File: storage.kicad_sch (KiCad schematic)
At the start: 18 parts, among them J6 Micro_SD_Card_Det1, U1 MIMX8MM6DVTLZAA, U25 TPD4EUSB30, U26 D5V0H1B2LP, U27 W25Q32JWZP, U28 SiP32431DR3, U29 TPD4EUSB30

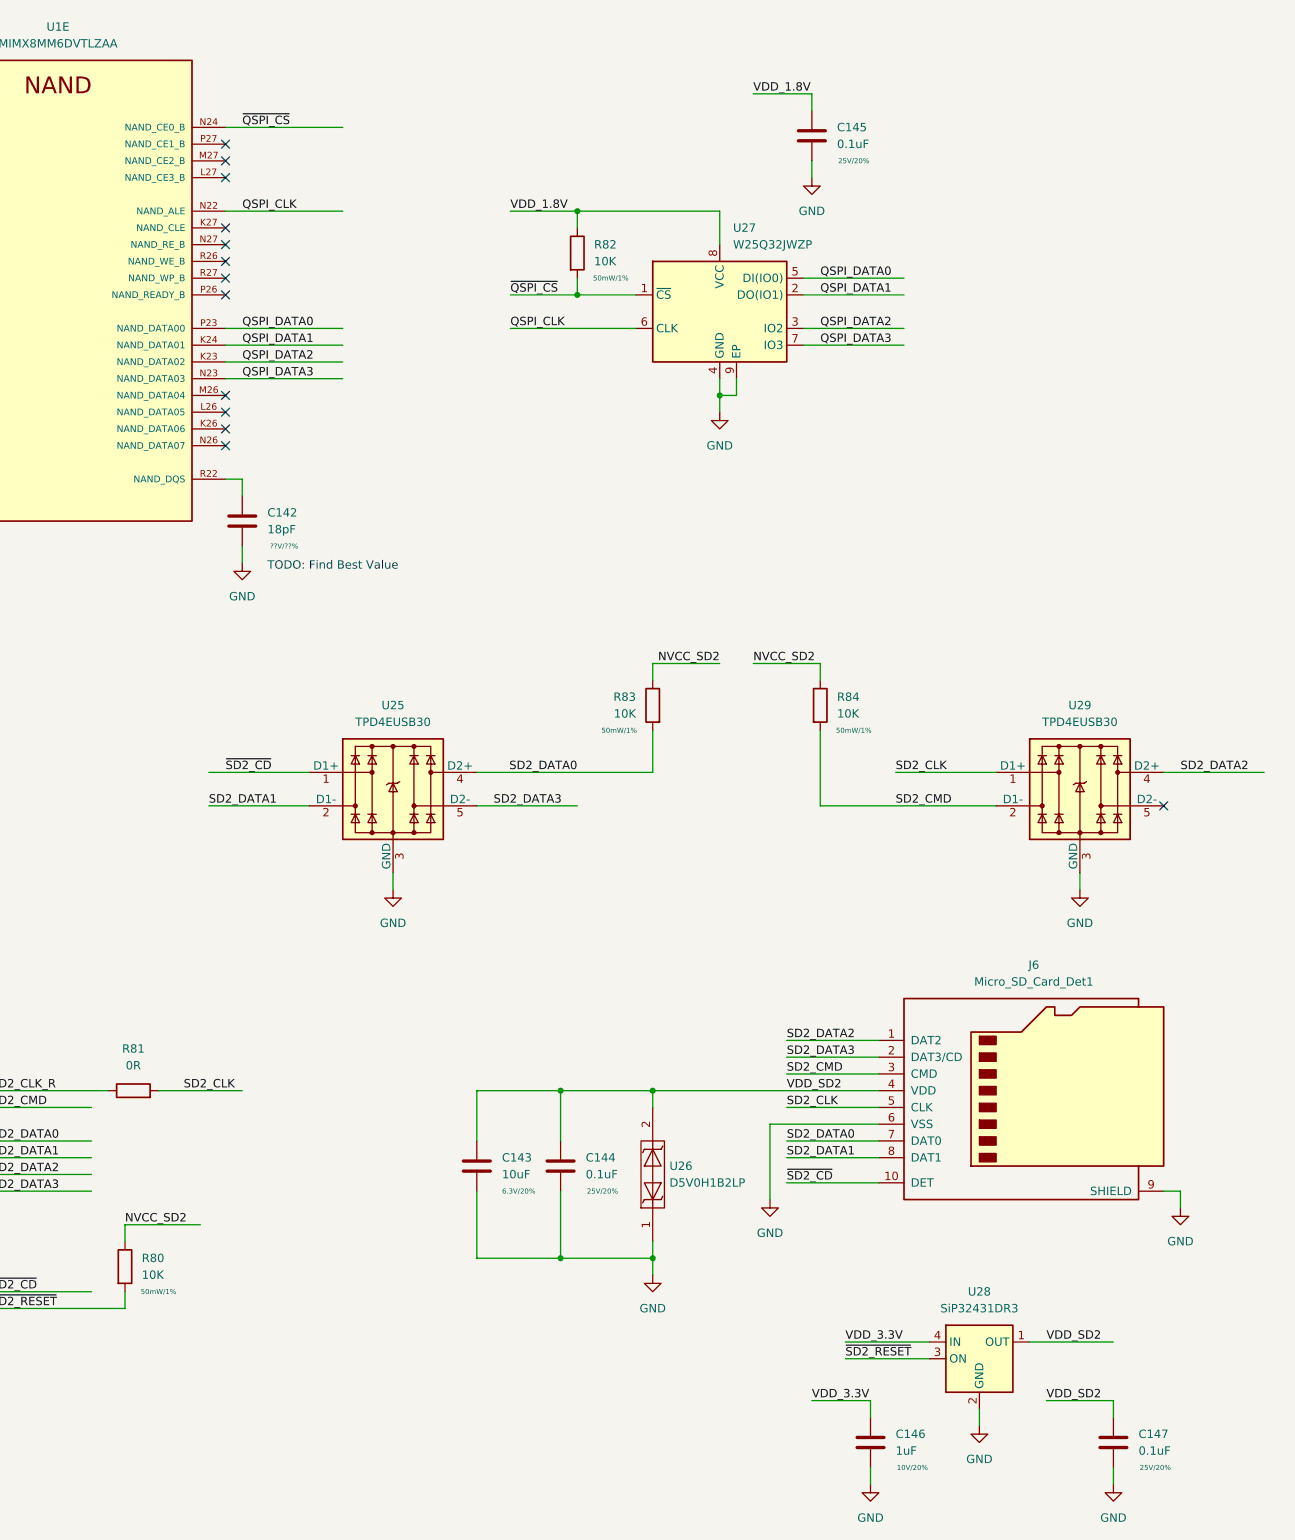
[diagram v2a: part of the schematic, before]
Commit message: inital routing of ddr data bus, sch work
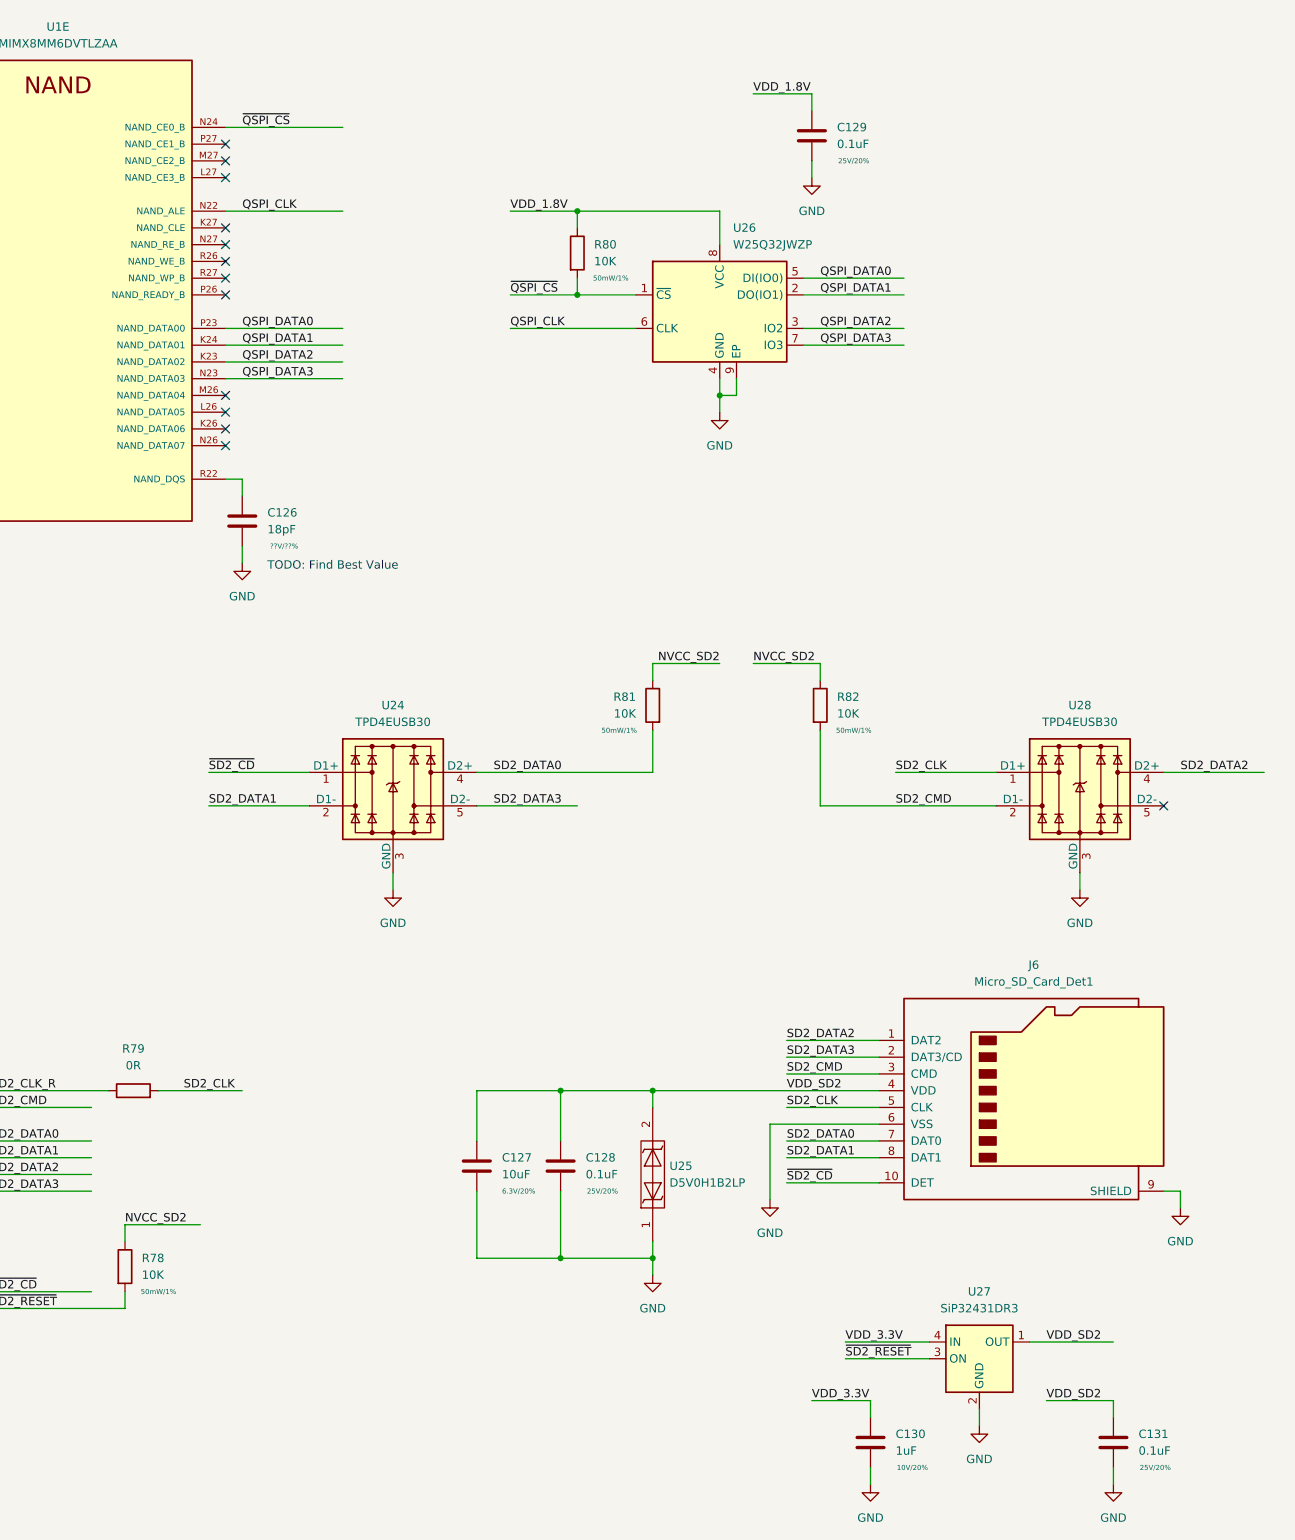
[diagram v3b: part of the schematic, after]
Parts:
- renumbered C142 to C126, C143 to C127, C144 to C128, C145 to C129, C146 to C130, C147 to C131, R80 to R78, R81 to R79, R82 to R80, R83 to R81, R84 to R82, U25 to U24, U26 to U25, U27 to U26, U28 to U27, U29 to U28
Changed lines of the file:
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@@
     (effects (font (size 1.27 1.27)) (justify left bottom))
   )
-  (label "~{SD2_CD}" (at 106.68 154.94 0)
+  (label "~{SD2_CD}" (at 104.14 154.94 0)
     (effects (font (size 1.27 1.27)) (justify left bottom))
   )
@@
     (effects (font (size 1.27 1.27)) (justify left bottom))
   )
-  (label "SD2_DATA0" (at 160.02 154.94 180)
-    (effects (font (size 1.27 1.27)) (justify right bottom))
+  (label "SD2_DATA0" (at 147.32 154.94 0)
+    (effects (font (size 1.27 1.27)) (justify left bottom))
   )
   (label "VDD_3.3V" (at 31.75 19.05 0)
@@
   (symbol (lib_id "Device:C") (at 144.78 214.63 0) (unit 1)
     (in_bom yes) (on_board yes)
-    (property "Reference" "C143" (id 0) (at 148.59 213.3599 0)
+    (property "Reference" "C127" (id 0) (at 148.59 213.3599 0)
       (effects (font (size 1.27 1.27)) (justify left))
     )
@@
   (symbol (lib_id "Device:R") (at 92.71 203.2 90) (unit 1)
     (in_bom yes) (on_board yes) (fields_autoplaced)
-    (property "Reference" "R81" (id 0) (at 92.71 196.85 90))
+    (property "Reference" "R79" (id 0) (at 92.71 196.85 90))
     (property "Value" "0R" (id 1) (at 92.71 199.39 90))
     (property "Footprint" "qsbc:R_0201_0603Metric" (id 2) (at 92.71 204.978 90)
@@
   (symbol (lib_id "power:GND") (at 195.58 64.77 0) (unit 1)
     (in_bom yes) (on_board yes) (fields_autoplaced)
-    (property "Reference" "#PWR0130" (id 0) (at 195.58 71.12 0)
+    (property "Reference" "#PWR0121" (id 0) (at 195.58 71.12 0)
       (effects (font (size 1.27 1.27)) hide)
     )
@@
   (symbol (lib_id "power:GND") (at 236.22 172.72 0) (unit 1)
     (in_bom yes) (on_board yes) (fields_autoplaced)
-    (property "Reference" "#PWR0133" (id 0) (at 236.22 179.07 0)
+    (property "Reference" "#PWR0124" (id 0) (at 236.22 179.07 0)
       (effects (font (size 1.27 1.27)) hide)
     )
@@
   (symbol (lib_id "Device:R") (at 171.45 144.78 0) (mirror y) (unit 1)
     (in_bom yes) (on_board yes)
-    (property "Reference" "R83" (id 0) (at 168.91 143.5099 0)
+    (property "Reference" "R81" (id 0) (at 168.91 143.5099 0)
       (effects (font (size 1.27 1.27)) (justify left))
     )
@@
   (symbol (lib_id "power:GND") (at 241.3 262.89 0) (unit 1)
     (in_bom yes) (on_board yes) (fields_autoplaced)
-    (property "Reference" "#PWR0134" (id 0) (at 241.3 269.24 0)
+    (property "Reference" "#PWR0125" (id 0) (at 241.3 269.24 0)
       (effects (font (size 1.27 1.27)) hide)
     )
@@
   (symbol (lib_id "power:GND") (at 251.46 220.98 0) (unit 1)
     (in_bom yes) (on_board yes) (fields_autoplaced)
-    (property "Reference" "#PWR0135" (id 0) (at 251.46 227.33 0)
+    (property "Reference" "#PWR0126" (id 0) (at 251.46 227.33 0)
       (effects (font (size 1.27 1.27)) hide)
     )
@@
   (symbol (lib_id "power:GND") (at 109.22 123.19 0) (unit 1)
     (in_bom yes) (on_board yes) (fields_autoplaced)
-    (property "Reference" "#PWR0125" (id 0) (at 109.22 129.54 0)
+    (property "Reference" "#PWR0116" (id 0) (at 109.22 129.54 0)
       (effects (font (size 1.27 1.27)) hide)
     )
@@
   (symbol (lib_id "Device:C") (at 204.47 256.54 0) (unit 1)
     (in_bom yes) (on_board yes)
-    (property "Reference" "C146" (id 0) (at 208.28 255.2699 0)
+    (property "Reference" "C130" (id 0) (at 208.28 255.2699 0)
       (effects (font (size 1.27 1.27)) (justify left))
     )
@@
   (symbol (lib_id "power:GND") (at 171.45 231.14 0) (unit 1)
     (in_bom yes) (on_board yes) (fields_autoplaced)
-    (property "Reference" "#PWR0127" (id 0) (at 171.45 237.49 0)
+    (property "Reference" "#PWR0118" (id 0) (at 171.45 237.49 0)
       (effects (font (size 1.27 1.27)) hide)
     )
@@
   (symbol (lib_id "power:GND") (at 189.23 219.71 0) (unit 1)
     (in_bom yes) (on_board yes) (fields_autoplaced)
-    (property "Reference" "#PWR0129" (id 0) (at 189.23 226.06 0)
+    (property "Reference" "#PWR0120" (id 0) (at 189.23 226.06 0)
       (effects (font (size 1.27 1.27)) hide)
     )
@@
   (symbol (lib_id "qsbc:TPD4EUSB30") (at 236.22 157.48 0) (unit 1)
     (in_bom yes) (on_board yes) (fields_autoplaced)
-    (property "Reference" "U29" (id 0) (at 236.22 144.78 0))
+    (property "Reference" "U28" (id 0) (at 236.22 144.78 0))
     (property "Value" "TPD4EUSB30" (id 1) (at 236.22 147.32 0))
     (property "Footprint" "Package_SON:USON-10_2.5x1.0mm_P0.5mm" (id 2) (at 212.09 167.64 0)
@@
   (symbol (lib_id "Memory_Flash:W25Q32JVZP") (at 181.61 85.09 0) (unit 1)
     (in_bom yes) (on_board yes) (fields_autoplaced)
-    (property "Reference" "U27" (id 0) (at 183.6294 72.39 0)
+    (property "Reference" "U26" (id 0) (at 183.6294 72.39 0)
       (effects (font (size 1.27 1.27)) (justify left))
     )
@@
   (symbol (lib_id "qsbc:D5V0H1B2LP") (at 170.18 215.9 90) (unit 1)
     (in_bom yes) (on_board yes) (fields_autoplaced)
-    (property "Reference" "U26" (id 0) (at 173.99 214.6299 90)
+    (property "Reference" "U25" (id 0) (at 173.99 214.6299 90)
       (effects (font (size 1.27 1.27)) (justify right))
     )
@@
   (symbol (lib_id "Device:R") (at 196.85 144.78 0) (unit 1)
     (in_bom yes) (on_board yes)
-    (property "Reference" "R84" (id 0) (at 199.39 143.5099 0)
+    (property "Reference" "R82" (id 0) (at 199.39 143.5099 0)
       (effects (font (size 1.27 1.27)) (justify left))
     )
@@
   (symbol (lib_id "Power_Management:SiP32431DR3") (at 220.98 243.84 0) (unit 1)
     (in_bom yes) (on_board yes) (fields_autoplaced)
-    (property "Reference" "U28" (id 0) (at 220.98 233.68 0))
+    (property "Reference" "U27" (id 0) (at 220.98 233.68 0))
     (property "Value" "SiP32431DR3" (id 1) (at 220.98 236.22 0))
     (property "Footprint" "Package_TO_SOT_SMD:SOT-363_SC-70-6" (id 2) (at 220.98 232.41 0)
@@
   (symbol (lib_id "power:GND") (at 204.47 262.89 0) (unit 1)
     (in_bom yes) (on_board yes) (fields_autoplaced)
-    (property "Reference" "#PWR0131" (id 0) (at 204.47 269.24 0)
+    (property "Reference" "#PWR0122" (id 0) (at 204.47 269.24 0)
       (effects (font (size 1.27 1.27)) hide)
     )
@@
   (symbol (lib_id "qsbc:TPD4EUSB30") (at 132.08 157.48 0) (unit 1)
     (in_bom yes) (on_board yes) (fields_autoplaced)
-    (property "Reference" "U25" (id 0) (at 132.08 144.78 0))
+    (property "Reference" "U24" (id 0) (at 132.08 144.78 0))
     (property "Value" "TPD4EUSB30" (id 1) (at 132.08 147.32 0))
     (property "Footprint" "Package_SON:USON-10_2.5x1.0mm_P0.5mm" (id 2) (at 107.95 167.64 0)
@@
   (symbol (lib_id "Device:C") (at 157.48 214.63 0) (unit 1)
     (in_bom yes) (on_board yes)
-    (property "Reference" "C144" (id 0) (at 161.29 213.3599 0)
+    (property "Reference" "C128" (id 0) (at 161.29 213.3599 0)
       (effects (font (size 1.27 1.27)) (justify left))
     )
@@
   (symbol (lib_id "Device:C") (at 195.58 58.42 0) (unit 1)
     (in_bom yes) (on_board yes)
-    (property "Reference" "C145" (id 0) (at 199.39 57.1499 0)
+    (property "Reference" "C129" (id 0) (at 199.39 57.1499 0)
       (effects (font (size 1.27 1.27)) (justify left))
     )
@@
   (symbol (lib_id "Device:R") (at 91.44 229.87 0) (unit 1)
     (in_bom yes) (on_board yes)
-    (property "Reference" "R80" (id 0) (at 93.98 228.5999 0)
+    (property "Reference" "R78" (id 0) (at 93.98 228.5999 0)
       (effects (font (size 1.27 1.27)) (justify left))
     )
@@
   (symbol (lib_id "Device:R") (at 160.02 76.2 0) (unit 1)
     (in_bom yes) (on_board yes)
-    (property "Reference" "R82" (id 0) (at 162.56 74.9299 0)
+    (property "Reference" "R80" (id 0) (at 162.56 74.9299 0)
       (effects (font (size 1.27 1.27)) (justify left))
     )
@@
   (symbol (lib_id "power:GND") (at 132.08 172.72 0) (unit 1)
     (in_bom yes) (on_board yes) (fields_autoplaced)
-    (property "Reference" "#PWR0126" (id 0) (at 132.08 179.07 0)
+    (property "Reference" "#PWR0117" (id 0) (at 132.08 179.07 0)
       (effects (font (size 1.27 1.27)) hide)
     )
@@
   (symbol (lib_id "power:GND") (at 181.61 100.33 0) (unit 1)
     (in_bom yes) (on_board yes) (fields_autoplaced)
-    (property "Reference" "#PWR0128" (id 0) (at 181.61 106.68 0)
+    (property "Reference" "#PWR0119" (id 0) (at 181.61 106.68 0)
       (effects (font (size 1.27 1.27)) hide)
     )
@@
   (symbol (lib_id "Device:C") (at 109.22 116.84 0) (unit 1)
     (in_bom yes) (on_board yes)
-    (property "Reference" "C142" (id 0) (at 113.03 115.5699 0)
+    (property "Reference" "C126" (id 0) (at 113.03 115.5699 0)
       (effects (font (size 1.27 1.27)) (justify left))
     )
@@
   (symbol (lib_id "power:GND") (at 220.98 254 0) (unit 1)
     (in_bom yes) (on_board yes) (fields_autoplaced)
-    (property "Reference" "#PWR0132" (id 0) (at 220.98 260.35 0)
+    (property "Reference" "#PWR0123" (id 0) (at 220.98 260.35 0)
       (effects (font (size 1.27 1.27)) hide)
     )
@@
   (symbol (lib_id "Device:C") (at 241.3 256.54 0) (unit 1)
     (in_bom yes) (on_board yes)
-    (property "Reference" "C147" (id 0) (at 245.11 255.2699 0)
+    (property "Reference" "C131" (id 0) (at 245.11 255.2699 0)
       (effects (font (size 1.27 1.27)) (justify left))
     )

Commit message: add SN65DSI86 DSI2DP ic, SCH, PCB work, flytime work
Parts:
- added C132: 4.7uF, Capacitor_SMD:C_0402_1005Metric, symbol Device:C
- added C133: 1uF, qsbc:C_0201_0603Metric, symbol Device:C
- added C134, C135, C136, C138, C139, C140: 0.22uF, qsbc:C_0201_0603Metric, symbol Device:C
- added C137: 10uF, Capacitor_SMD:C_0402_1005Metric, symbol Device:C
- added R81, R85: 0R, qsbc:R_0201_0603Metric, symbol Device:R
- added R84, R86, R87: 10K, Resistor_SMD:R_0402_1005Metric, symbol Device:R
- added U29: EMMC, qsbc:FBGA-153, symbol qsbc:EMMC
- renumbered C129 to C128, C128 to C129, R81 to R80, R80 to R82, R82 to R83, U26 to U25, U28 to U26, U25 to U27, U27 to U28
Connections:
- net GND: now also C132.2, C133.2, C134.2, C135.2, C136.2, C137.2, C138.2, C139.2, C140.2, U29.A6 (VSS1), U29.C4 (VSSQ1), U29.E7 (VSS2), U29.G5 (VSS3), U29.H10 (VSS4), U29.J5 (VSS5), U29.K8 (VSS6), U29.N2 (VSSQ2), U29.N5 (VSSQ3), U29.P4 (VSSQ4), U29.P6 (VSSQ5)
- net VDD_1.8V: now also C137.1, C138.1, C139.1, C140.1, R84.1, R86.1, R87.1, U29.C6 (VCCQ1), U29.M4 (VCCQ2), U29.N4 (VCCQ3), U29.P3 (VCCQ4), U29.P5 (VCCQ5)
- net VDD_3.3V: now also C132.1, C134.1, C136.1, U29.E6 (VCC1), U29.F5 (VCC2), U29.J10 (VCC3), U29.K9 (VCC4)
- net SD3_DATA2: now reaches U1.K26 (NAND_DATA06)
- net SD3_DATA2: now also U29.A5 (DAT2)
- net SD3_DATA7: now reaches U1.K27 (NAND_CLE)
- net SD3_DATA7: now also U29.B6 (DAT7)
- net SD3_DATA1: now reaches U1.L26 (NAND_DATA05)
- net SD3_DATA1: now also U29.A4 (DAT1)
- net SD3_DATA6: now reaches U1.L27 (NAND_CE3_B)
- net SD3_DATA6: now also U29.B5 (DAT6)
- net SD3_DATA0: now reaches U1.M26 (NAND_DATA04)
- net SD3_DATA0: now also R87.2, U29.A3 (DAT0)
- net SD3_DATA5: now reaches U1.M27 (NAND_CE2_B)
- net SD3_DATA5: now also U29.B4 (DAT5)
- net SD3_DATA3: now reaches U1.N26 (NAND_DATA07)
- net SD3_DATA3: now also U29.B2 (DAT3)
- net SD3_DATA4: now reaches U1.N27 (NAND_RE_B)
- net SD3_DATA4: now also U29.B3 (DAT4)
- net ~{SD3_RESET}: now reaches U1.P26 (NAND_READY_B)
- net ~{SD3_RESET}: now also R85.1
- net SD3_STROBE: now reaches U1.P27 (NAND_CE1_B)
- net SD3_STROBE: now also U29.H5 (DS)
- net SD3_CLK_R: now reaches U1.R26 (NAND_WE_B)
- net SD3_CLK_R: now also R81.1
- net SD3_CMD: now reaches U1.R27 (NAND_WP_B)
- net SD3_CMD: now also R84.2, U29.M5 (CMD)
- net ~{QSPI_CS} renamed ~{QSPI_CS0}
- new net SD3_CLK: R81.2, U29.M6 (CLK)
- new net eMMC_VDDI: C133.1, C135.1, U29.C2 (VDDI)
- new net ~{SD3_RESET_R}: R85.2, R86.2, U29.K5 (~{RST})
- no-connect marks 26 -> 134
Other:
- moved on the sheet: C126, C128, R80, R82, R83, U1E, U1J, U24, U25, U26
